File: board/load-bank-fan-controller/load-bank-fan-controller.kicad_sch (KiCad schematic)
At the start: 42 parts, among them J1 UART, J10 Conn Relay, J11 Conn Temp, J12 Conn Temp, J13 Conn Temp, J2 FAN1, J3 FAN2, J4 FAN3, J5 FAN4, J6 Conn 12V, J7 SJ-3523-SMT-TR, J8 SJ-3523-SMT-TR, J9 SJ-3523-SMT-TR, Q1 IRF540N, SW1 SW_Push, U1 ATmega328P-A, U2 AMS1117-5.0, Y1 Crystal

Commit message: finish board routing
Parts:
- removed J13: Conn Temp, Connector_Molex:Molex_KK-254_AE-6410-02A_1x02_P2.54mm_Vertical, symbol Connector:Conn_01x02_Pin
- removed J5: FAN4, Connector:FanPinHeader_1x04_P2.54mm_Vertical, symbol Connector:Conn_01x04_Pin
- removed J7, J8, J9: SJ-3523-SMT-TR, SJ-3523-SMT-TR:CUI_SJ-3523-SMT-TR, symbol SJ-3523-SMT-TR:SJ-3523-SMT-TR
- removed R12: 1K, Resistor_SMD:R_0603_1608Metric_Pad0.98x0.95mm_HandSolder, symbol Device:R
- removed R5, R6, R7, R8: 4K7, Resistor_SMD:R_0603_1608Metric_Pad0.98x0.95mm_HandSolder, symbol Device:R
- added H1, H2, H3: MountingHole, MountingHole:MountingHole_3.2mm_M3, symbol Mechanical:MountingHole
- added J4: CT, Connector_JST:JST_XH_B3B-XH-A_1x03_P2.50mm_Vertical, symbol Connector:Conn_01x03_Pin
- added R4: 10K, Resistor_SMD:R_0603_1608Metric_Pad0.98x0.95mm_HandSolder, symbol Device:R
- J1: renamed from J2; footprint Connector:FanPinHeader_1x04_P2.54mm_Vertical -> Connector_Molex:Molex_KK-254_AE-6410-04A_1x04_P2.54mm_Vertical
- J2: renamed from J3; footprint Connector:FanPinHeader_1x04_P2.54mm_Vertical -> Connector_Molex:Molex_KK-254_AE-6410-04A_1x04_P2.54mm_Vertical
- J3: renamed from J4; footprint Connector:FanPinHeader_1x04_P2.54mm_Vertical -> Connector_Molex:Molex_KK-254_AE-6410-04A_1x04_P2.54mm_Vertical
- J5: renamed from J1; footprint Connector_Molex:Molex_KK-254_AE-6410-04A_1x04_P2.54mm_Vertical -> Connector_JST:JST_XH_B4B-XH-A_1x04_P2.50mm_Vertical
- J7: renamed from J11; value Conn Temp -> TEMP1; footprint Connector_Molex:Molex_KK-254_AE-6410-02A_1x02_P2.54mm_Vertical -> Connector_JST:JST_XH_B2B-XH-A_1x02_P2.50mm_Vertical
- J8: renamed from J12; value Conn Temp -> TEMP2; footprint Connector_Molex:Molex_KK-254_AE-6410-02A_1x02_P2.54mm_Vertical -> Connector_JST:JST_XH_B2B-XH-A_1x02_P2.50mm_Vertical
- R3: renamed from R9; value 330 -> 100; LCSC PN C105881 -> C105588; Mfg PN RC0603FR-07330RL -> RC0603FR-07100RL
- SW1: value SW_Push -> RESET
- renumbered C5 to C1, C6 to C2, C7 to C3, C8 to C4, C3 to C5, C1 to C6, C2 to C7, C4 to C8, D2 to D1, D1 to D2, J10 to J9, R3 to R1, R4 to R2, R10 to R5, R11 to R6, R1 to R7, R2 to R8, U2 to U1, U1 to U2
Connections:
- net CT1 is gone; now on net TEMP1: U2.23 (PC0)
- net CT2 is gone; now on net TEMP2: U2.24 (PC1)
- net +12V: now also J1.2 (Pin_2), J2.2 (Pin_2), J3.2 (Pin_2); no longer J1.3 (Pin_3), J2.3 (Pin_3), J3.3 (Pin_3)
- net FAN1_FB: now also J1.3 (Pin_3); no longer J1.2 (Pin_2)
- net FAN2_FB: now also J2.3 (Pin_3); no longer J2.2 (Pin_2)
- net FAN3_FB: now also J3.3 (Pin_3); no longer J3.2 (Pin_2)
- net FAN_PWM: now also J1.4 (Pin_4), J2.4 (Pin_4), J3.4 (Pin_4); no longer J1.1 (Pin_1), J2.1 (Pin_1), J3.1 (Pin_1)
- net GND: now also J1.1 (Pin_1), J2.1 (Pin_1), J3.1 (Pin_1), J5.1 (Pin_1), R4.2; no longer J1.4 (Pin_4), J2.4 (Pin_4), J3.4 (Pin_4), J5.4 (Pin_4)
- net TEMP1: no longer U2.26 (PC3)
- net TEMP2: no longer U2.27 (PC4)
- net at D1.2 (A): now also J5.4 (Pin_4); no longer J5.1 (Pin_1)
- net at Q1.1 (G), R3.2: now also R4.1
- net at R1.1, R2.1: now also J4.1 (Pin_1)
- net CT3 renamed CT
- net CT: now also J4.3 (Pin_3)
- net FAN4_FB renamed D5
- net TEMP3 renamed A5
- new net A3: U2.26 (PC3)
- new net A4: U2.27 (PC4)
- no-connect marks 3 -> 1
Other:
- note added: "MCU"
- note removed: "Fan 4"
- note removed: "Temperature 3"
- note removed: "uC"
- moved on the sheet: C1, C10, C2, C3, C4, C5, C6, C7, C8, C9, D1, D2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

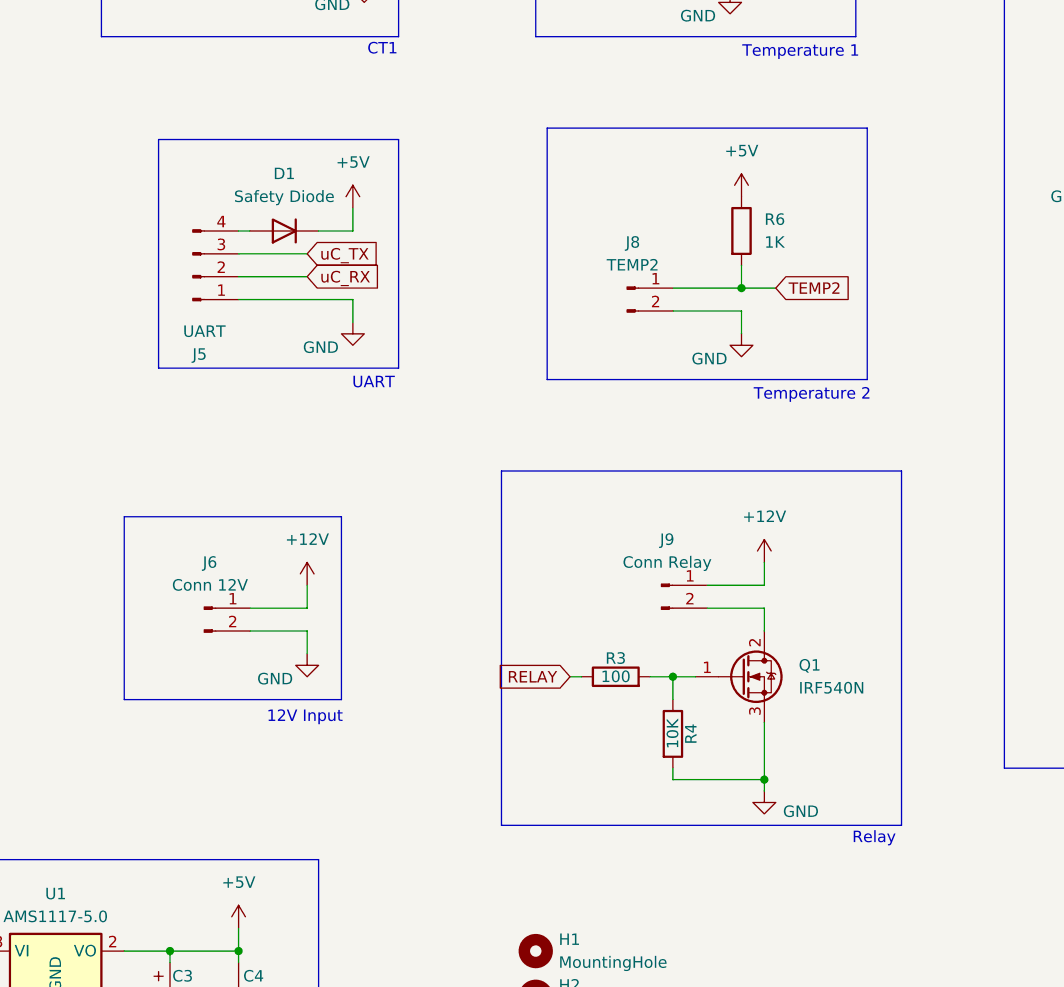
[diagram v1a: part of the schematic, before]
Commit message: change pin assignment
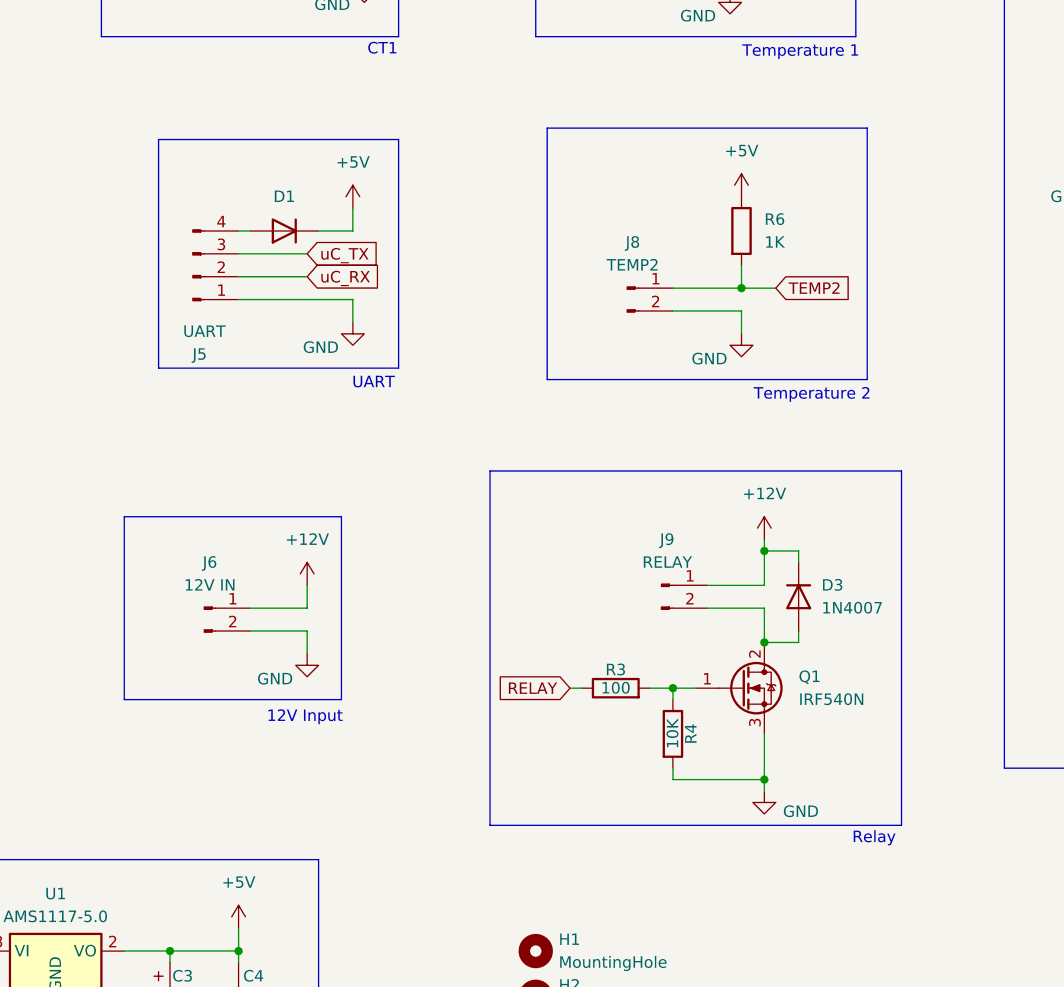
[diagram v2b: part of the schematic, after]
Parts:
- added D3: 1N4007, Diode_SMD:D_SOD-123F, symbol Device:D
- C1, C3, C8: LCSC PN C14664 -> (none); LCSC Part # (none) -> C14664
- C10, C9: LCSC PN C105620 -> (none); LCSC Part # (none) -> C105620
- C2, C4, C5, C6: LCSC PN C92490 -> (none); LCSC Part # (none) -> C92490
- C7: LCSC PN C326580 -> (none); LCSC Part # (none) -> C326580
- D1: LCSC PN C145179 -> (none); LCSC Part # (none) -> C145179
- D2: LCSC PN C125093 -> (none); LCSC Part # (none) -> C125093
- H1, H2, H3: LCSC PN C7429633 -> (none); Manufacturer Megastar -> (none); Mfg PN ZX-XH2.54-3PZZ -> (none)
- J1, J2, J3: LCSC PN C240840 -> (none); LCSC Part # (none) -> C240840
- J4: LCSC Part # (none) -> C7429633; Manufacturer (none) -> Megastar; Mfg PN (none) -> ZX-XH2.54-3PZZ
- J5: LCSC PN C2908613 -> (none); LCSC Part # (none) -> C7429634; Mfg PN XH-4AW -> ZX-XH2.54-4PZZ
- J6: value Conn 12V -> 12V IN; footprint TerminalBlock:TerminalBlock_bornier-2_P5.08mm -> TerminalBlock_RND:TerminalBlock_RND_205-00232_1x02_P5.08mm_Horizontal; LCSC PN C8465 -> (none); LCSC Part # (none) -> C8465
- J7, J8: LCSC PN C7429632 -> (none); LCSC Part # (none) -> C7429632
- J9: value Conn Relay -> RELAY; footprint TerminalBlock:TerminalBlock_bornier-2_P5.08mm -> TerminalBlock_RND:TerminalBlock_RND_205-00232_1x02_P5.08mm_Horizontal; LCSC PN C8465 -> (none); LCSC Part # (none) -> C8465
- Q1: LCSC PN C2566 -> (none); LCSC Part # (none) -> C2566
- R1, R2: LCSC PN C99782 -> (none); LCSC Part # (none) -> C99782
- R3: LCSC PN C105588 -> (none); LCSC Part # (none) -> C105588
- R4: LCSC PN C98220 -> (none); LCSC Part # (none) -> C98220
- R5, R6, R7: LCSC PN C22548 -> (none); LCSC Part # (none) -> C22548
- R8: LCSC PN C105881 -> (none); LCSC Part # (none) -> C105881
- SW1: LCSC PN C318938 -> (none); LCSC Part # (none) -> C318938
- U1: LCSC PN C6187 -> (none); LCSC Part # (none) -> C6187
- U2: LCSC PN C14877 -> (none); LCSC Part # (none) -> C14877
- Y1: LCSC PN C16212 -> (none); LCSC Part # (none) -> C16212
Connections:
- net +12V: now also D3.1 (K)
- net at J9.2 (Pin_2), Q1.2 (D): now also D3.2 (A)
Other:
- moved on the sheet: Q1, R3
